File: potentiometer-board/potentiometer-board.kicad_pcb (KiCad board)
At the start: 2 copper layers, 27.3 x 27.3 mm, 7 parts, among them J1 Conn_01x03

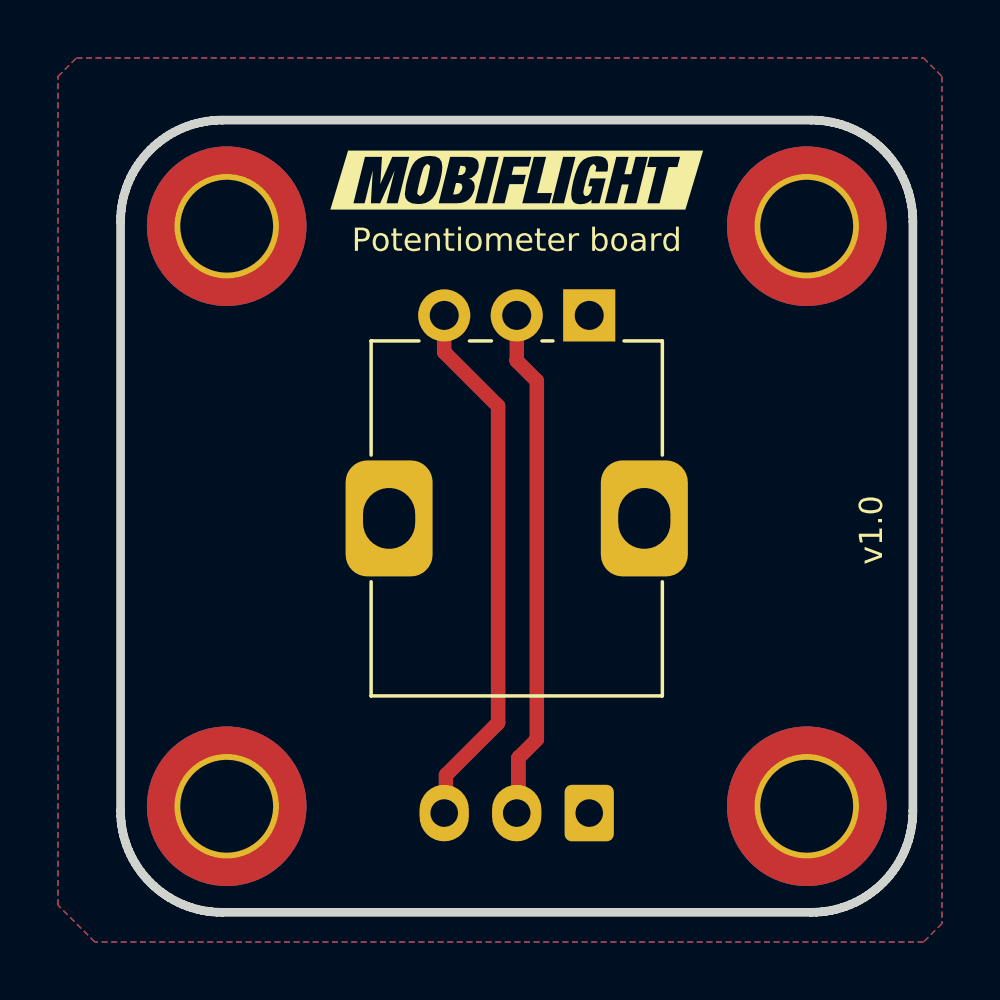
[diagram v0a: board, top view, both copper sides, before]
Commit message: Update all boards to KiCad 9.0 (#44)
* update dimmer board to KiCad version 9

* update dual encoder board to KiCad version 9

* update input shifter board, start numbering with zero instead one

* update MAX7219 breakout board to KiCad version 9

* add 3 pol JST connector

* updatge template to KiCad version 9

* update potentiometer board to KiCad version 9, use JST connector from MF lib

* update 6pin JST connector

* update prototyping board to KiCad version 9

* update symbols on dimmer board, fixed DRC

* update symbols from MAX7219 breakout board

* add Screw Terminalblocks to footprint lib and 3D models

* use screw terminals from MF lib

* fixed outline of Potentiometer board

* fixed missing IDC footprints error

* add MAX7219 symbol

* use MAX7219 symbol from MF lib

* add Mega2560mini symbol and footprint to MF library

* use Mega2560mini symbol and footprint from MF library

* add used Dual Encoder symbol and footprint to MF lib

* use footprint and symbol for Dual Encoder from MF lib
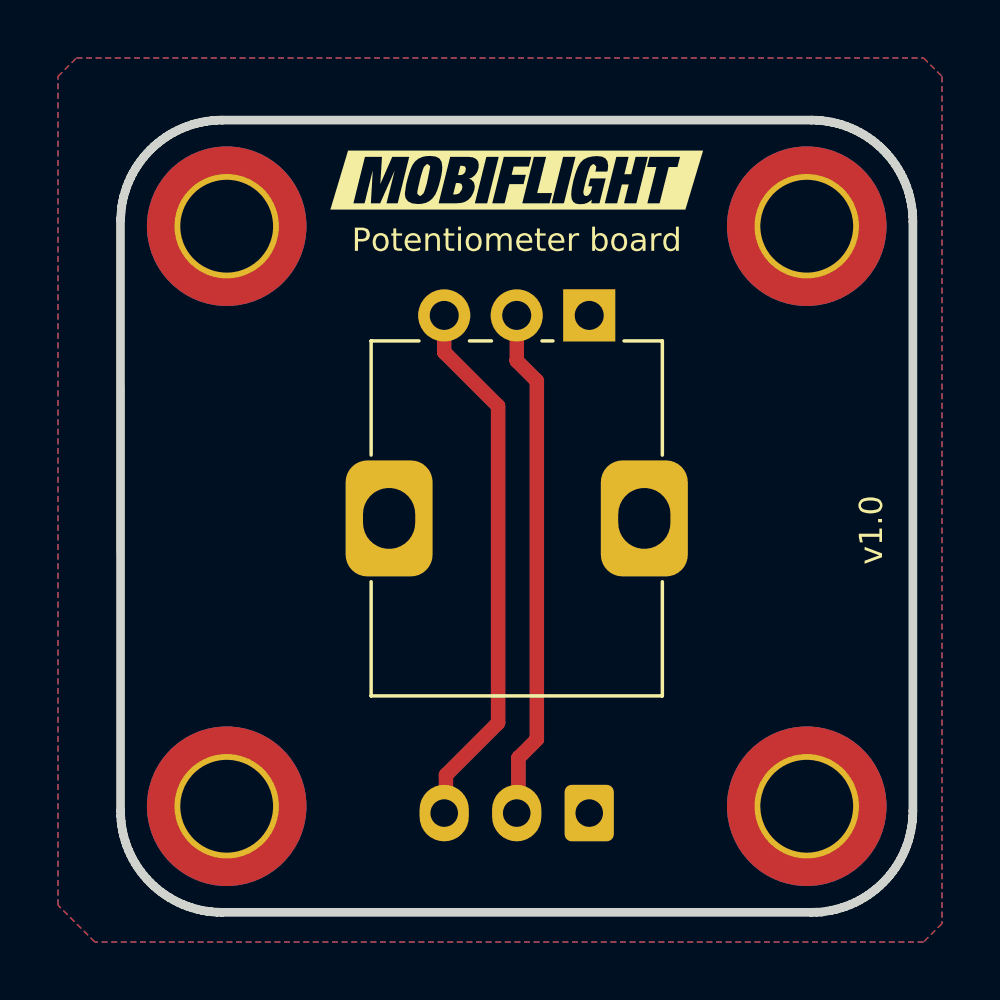
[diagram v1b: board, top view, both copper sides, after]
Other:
- outline, holes or cut-outs redrawn
